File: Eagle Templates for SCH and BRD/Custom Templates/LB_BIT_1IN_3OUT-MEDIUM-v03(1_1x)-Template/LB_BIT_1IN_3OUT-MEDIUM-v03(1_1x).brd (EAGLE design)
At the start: 74.2 x 18.2 mm, 25 parts, among them U1 LV321SOT23-5, U2 LV321SOT23-5, U3 LV321SOT23-5, U6 LV321SOT23-5

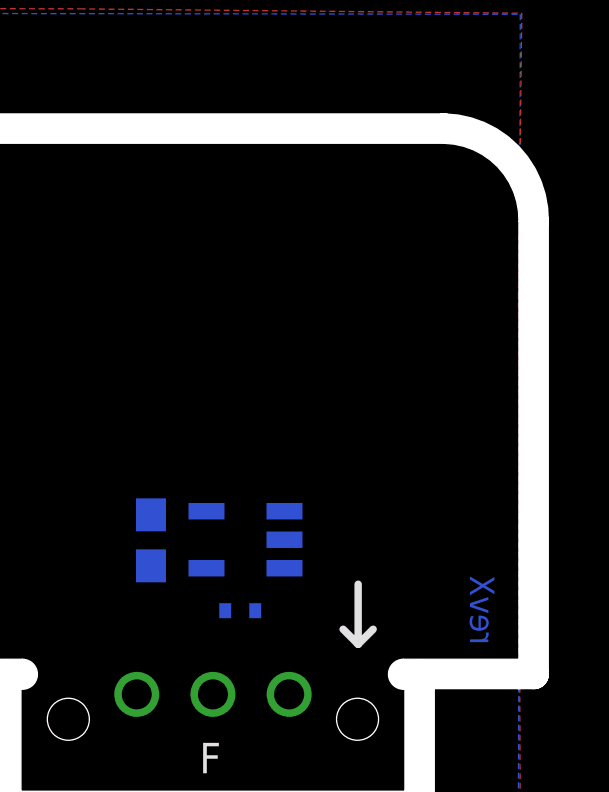
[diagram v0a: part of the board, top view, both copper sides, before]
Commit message: added bitlab logo and made minor changes to board templates. Updated littlebits library.
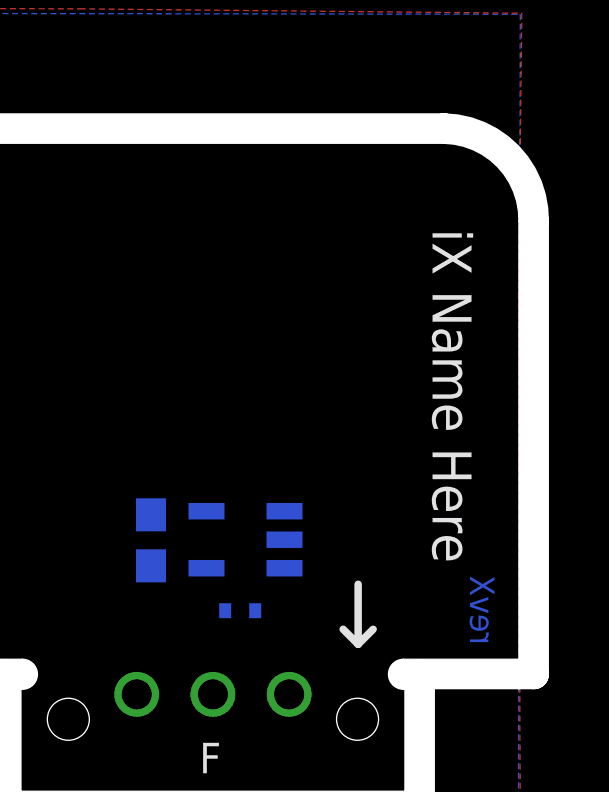
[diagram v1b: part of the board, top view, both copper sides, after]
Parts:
- added U$1: (no value), LITTLEBITS:BITLAB-LOGO
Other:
- board text added: "iX Name Here"
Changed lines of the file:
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@@
 <wire x1="50.33" y1="17.32" x2="49.83" y2="17.32" width="1" layer="46"/>
 <text x="48.2" y="18.3" size="0.8128" layer="16" font="vector" ratio="12" rot="MR90">revX</text>
+<text x="47.6" y="26.6" size="1.3" layer="21" font="vector" rot="SR270" align="center">iX Name Here</text>
 </plain>
 <attributes>
@@
 <element name="U$2" library="LITTLEBITS" package="OSHWCREDIT" value="OSHWCREDIT" x="-94.025" y="-60.81"/>
 <element name="FRAME1" library="LITTLEBITS" package="FABDWG01-OHW" value="FRAME-LETTER" x="0" y="0"/>
+<element name="U$1" library="LITTLEBITS" package="BITLAB-LOGO" value="" x="45.5" y="28.1" rot="R270"/>
 </elements>
 <signals>

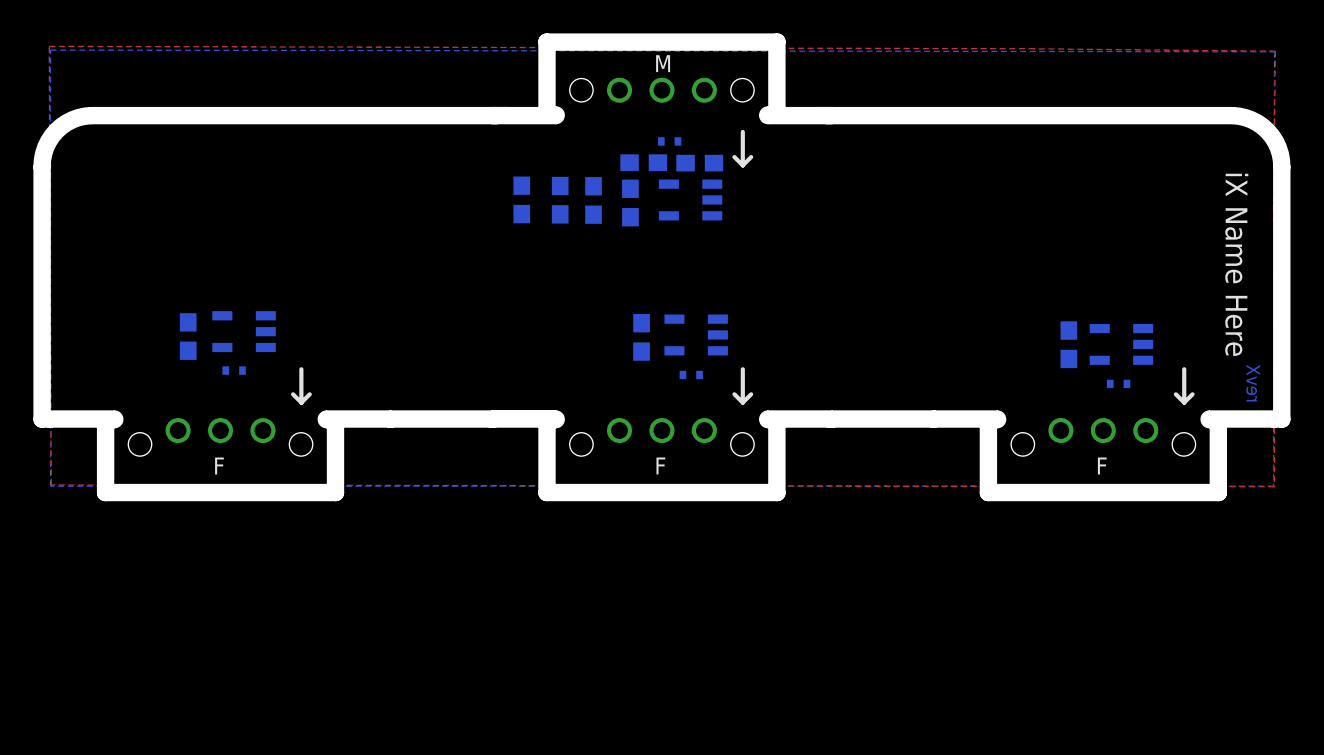
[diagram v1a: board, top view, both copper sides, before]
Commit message: Updated templates
- Added ferrite beads
- Moved text and annotations off of Nets layer
- Minor layout changes
- Removed I/O/W prefix from reference designators
- Removed output stage components from output bits
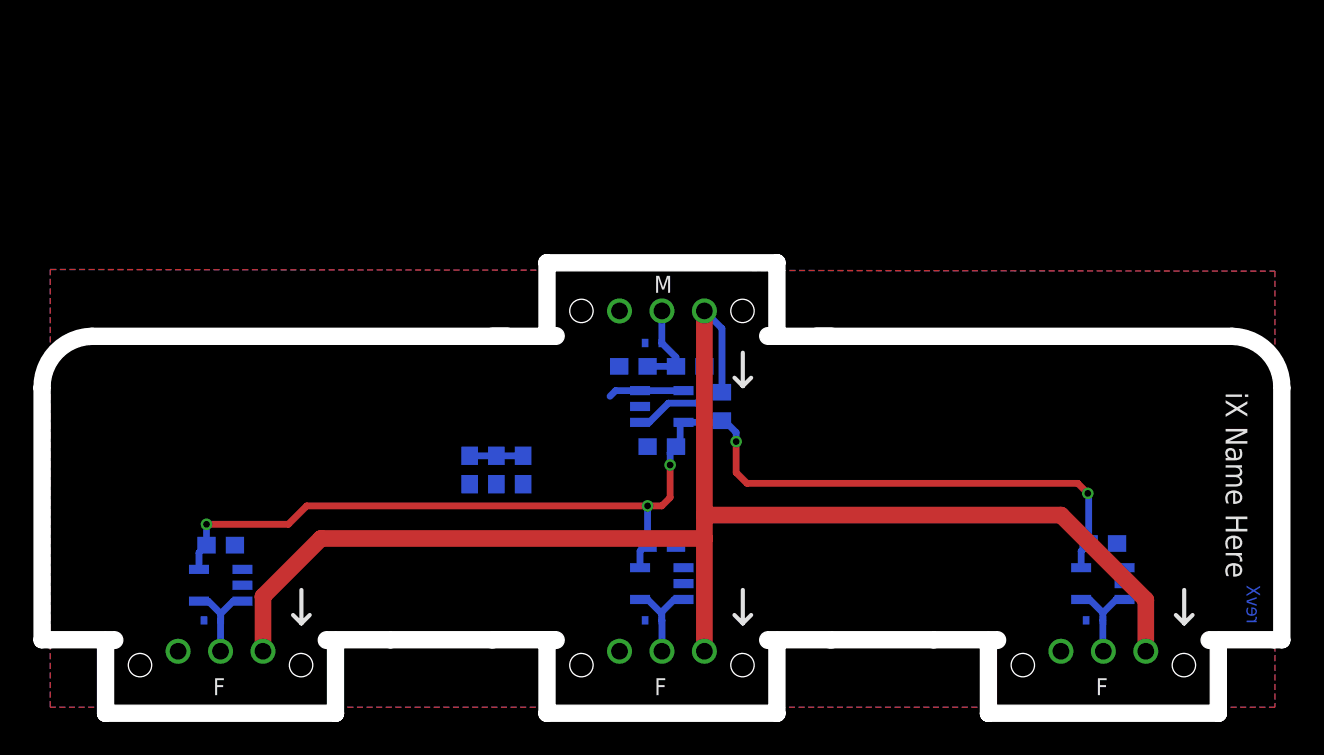
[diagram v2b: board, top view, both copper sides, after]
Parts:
- removed I?C1: 0.1uF, LITTLEBITS:CAP-0603
- removed I?C2: 10uF, LITTLEBITS:CAP-0603
- removed I?C3, I?C4, I?C5: 1.0uF, LITTLEBITS:CAP-0603
- removed I?R1: 1meg, LITTLEBITS:RES-0603
- removed I?R2: 10K, LITTLEBITS:RES-0603
- removed I?R3, I?R4: 3K3, LITTLEBITS:RES-0603
- removed I?TVS1, I?TVS2, I?TVS3, I?TVS6: ESD9B5.0ST5G, LITTLEBITS:SOD-923
- removed U6: LV321SOT23-5, LITTLEBITS:SOT23-5
- removed W11BSF1, W11BSF2, W11BSF3: BITSNAP_V03_FEMALE, bitSnap:BITSNAP_V03_FEMALE
- removed W11BSM1: BITSNAP_V03_MALE, bitSnap:BITSNAP_V03_MALE
- added BSF1, BSF2, BSF3: BITSNAP_V03_FEMALE, bitSnap:BITSNAP_V03_FEMALE
- added BSM1: BITSNAP_V03_MALE, bitSnap:BITSNAP_V03_MALE
- added C1: 0.1uF, LITTLEBITS:CAP-0603
- added C2: 10uF, LITTLEBITS:CAP-0603
- added C3, C4, C5: 1.0uF, LITTLEBITS:CAP-0603
- added FB1: FERRITE-BEAD0603, LITTLEBITS:R0603
- added R1: 1meg, LITTLEBITS:RES-0603
- added R2: 10K, LITTLEBITS:RES-0603
- added R3, R4: 3K3, LITTLEBITS:RES-0603
- added TVS1, TVS2, TVS3, TVS4: ESD9B5.0ST5G, LITTLEBITS:SOD-923
- added U4: LV321SOT23-5, LITTLEBITS:SOT23-5
- moved U3 55.8 mm to (-13.2, 7.39)
- moved U2 29.2 mm to (13.2, 7.49)
- moved U$1 13.2 mm to (45.5, 14.9)
- moved U$21 13.2 mm to (45.0, 15.7)
- moved U1 12.5 mm to (13.2, 18.1), turned to 90 degrees
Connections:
- new net LB_VCC: BSF1.VCC, BSF2.VCC, BSF3.VCC, BSM1.VCC1, FB1.2
- net GND: now also BSF1.GND, BSF2.GND, BSF3.GND, BSM1.GND1, C1.2, C2.2, C3.1, C4.1, C5.1, R1.1, R4.1, TVS1.1, TVS2.1, TVS3.1, TVS4.1, U4.2; no longer I?C1.2, I?C2.2, I?C3.1, I?C4.1, I?C5.1, I?R1.1, I?R4.1, I?TVS1.1, I?TVS2.1, I?TVS3.1, I?TVS6.1, U6.2, W11BSF2.GND, W11BSF3.GND, W11BSM1.GND1
- net N$12: now also U4.1; no longer U6.1
- net N$4: now also R2.1; no longer I?R2.1
- net SIG_OUT: now also BSM1.SIG1, R1.2, R2.2, TVS1.2; no longer I?R1.2, I?R2.2, I?TVS1.2, W11BSM1.SIG1
- net SIG_OUT1: now also BSF1.SIG, TVS4.2, U4.3, U4.4; no longer I?TVS6.2, U6.3, U6.4
- net SIG_OUT2: now also BSF2.SIG, TVS2.2; no longer I?TVS2.2, W11BSF2.SIG
- net SIG_OUT3: now also BSF3.SIG, TVS3.2; no longer I?TVS3.2, W11BSF3.SIG
- net VCC: now also C1.1, C3.2, C4.2, C5.2, FB1.1, R3.2, U4.5; no longer I?C1.1, I?C3.2, I?C4.2, I?C5.2, I?R3.2, U6.5, W11BSF2.VCC, W11BSF3.VCC, W11BSM1.VCC1
- net VREF: now also C2.1, R3.1, R4.2; no longer I?C2.1, I?R3.1, I?R4.2
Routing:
- net LB_VCC: track 0.00 -> 88.4 mm
- net VCC: track 0.00 -> 72.3 mm, vias 0 -> 5
- net N$4: track 0.00 -> 6.35 mm
- net SIG_OUT2: track 0.00 -> 5.59 mm
- net SIG_OUT1: track 0.00 -> 5.58 mm
- net SIG_OUT3: track 0.00 -> 5.48 mm
- net SIG_OUT: track 0.00 -> 5.38 mm
- net N$3: track 0.00 -> 4.54 mm
- net VREF: track 0.00 -> 3.20 mm
- added copper zone on layer 1, net GND
- removed copper zone on layer 1, net GND_BIT
